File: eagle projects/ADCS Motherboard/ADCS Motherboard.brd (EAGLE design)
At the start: 91 x 91 mm, 144 parts, among them J1 HDR_10_EZFET_DEBUGGER, J11 CNC_3221-10-0300-00, J5 CNC_3221-10-0300-00, J7 TE-1734829-3, Q1 BSR802NL6327HTSA1, U1 MSP430F5529IPN, U10 TSV991AILT, U2 TSV991AILT, U3 ADS7841E_2K5, U4 TSV991AILT, U5 DMC4050SSDQ-13, U6 BNO055, U7 HMC1053, U9 BMX160, Y1 32.768kHz, Y2 CSTCR4M00G15L99, Y3 32.768kHz

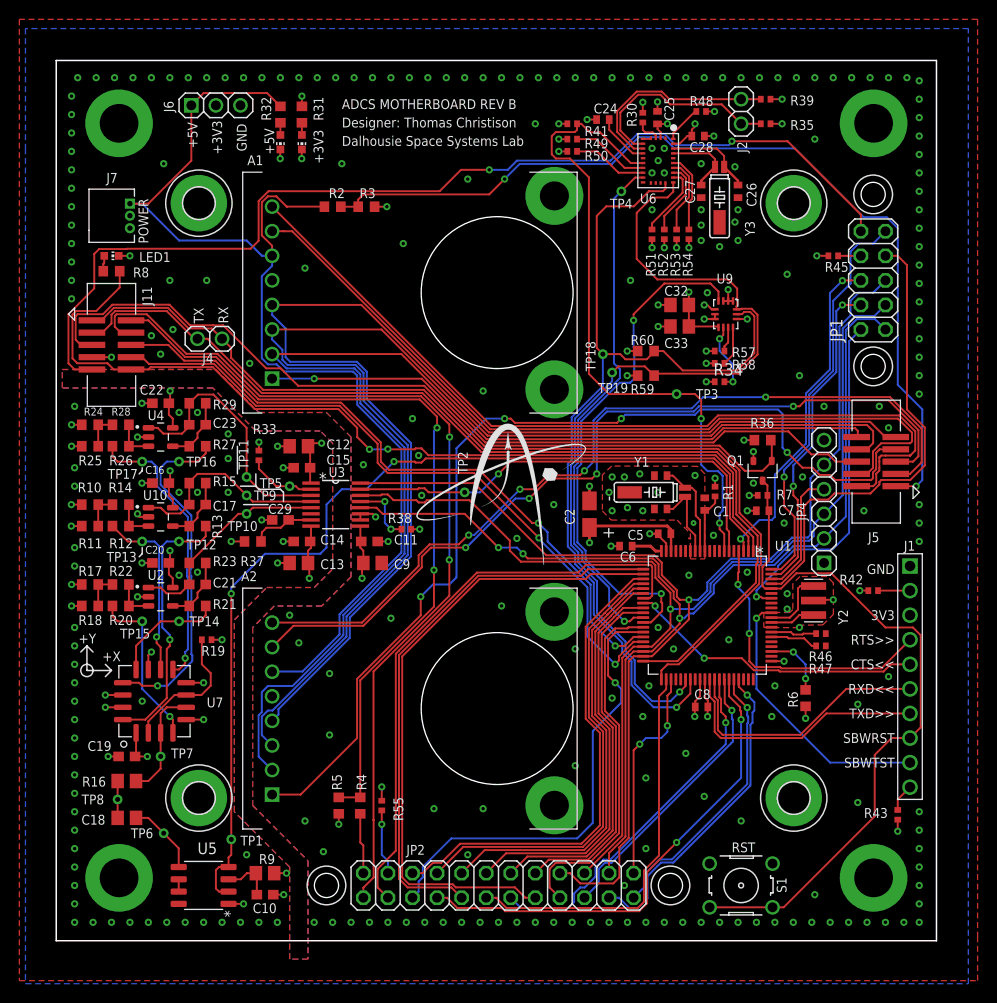
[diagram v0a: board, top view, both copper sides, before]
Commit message: silk screen
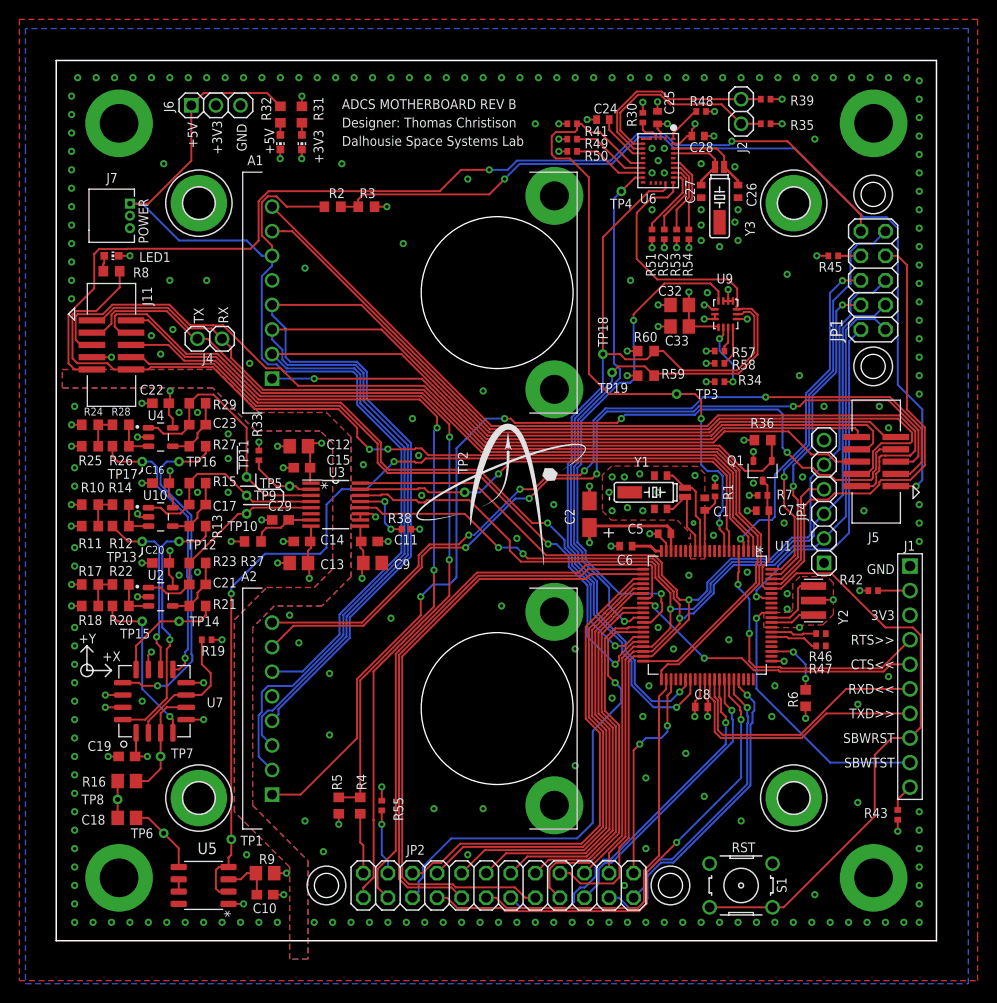
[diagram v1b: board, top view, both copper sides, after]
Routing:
- net UCB1_I2C_SCL: track 94.8 -> 92.6 mm
- net RESERVED_2: track 71.5 -> 72.2 mm
- net RESERVED_1: track 70.2 -> 70.7 mm

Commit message: finilized rev b layout
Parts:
- moved J6 16.6 mm to (14.6, 69.8), turned to 180 degrees
- moved R31 8.04 mm to (17.5, 84.1), turned to 0 degrees
- moved R32 6.70 mm to (17.5, 81.9), turned to 0 degrees
- moved LED2 5.32 mm to (20.3, 84.1), turned to 270 degrees
- moved LED3 2.93 mm to (20.3, 81.9), turned to 270 degrees
- moved LED1 0.95 mm to (4.76, 70.8)
- moved R8 0.95 mm to (4.76, 69.2)
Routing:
- net +5V: track 115.8 -> 105.6 mm
- net Z-_SUN_3V_PRESENT: track 107.5 -> 108.0 mm
- net GND: vias 311 -> 317
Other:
- outline, holes or cut-outs redrawn
- board text added: "*"

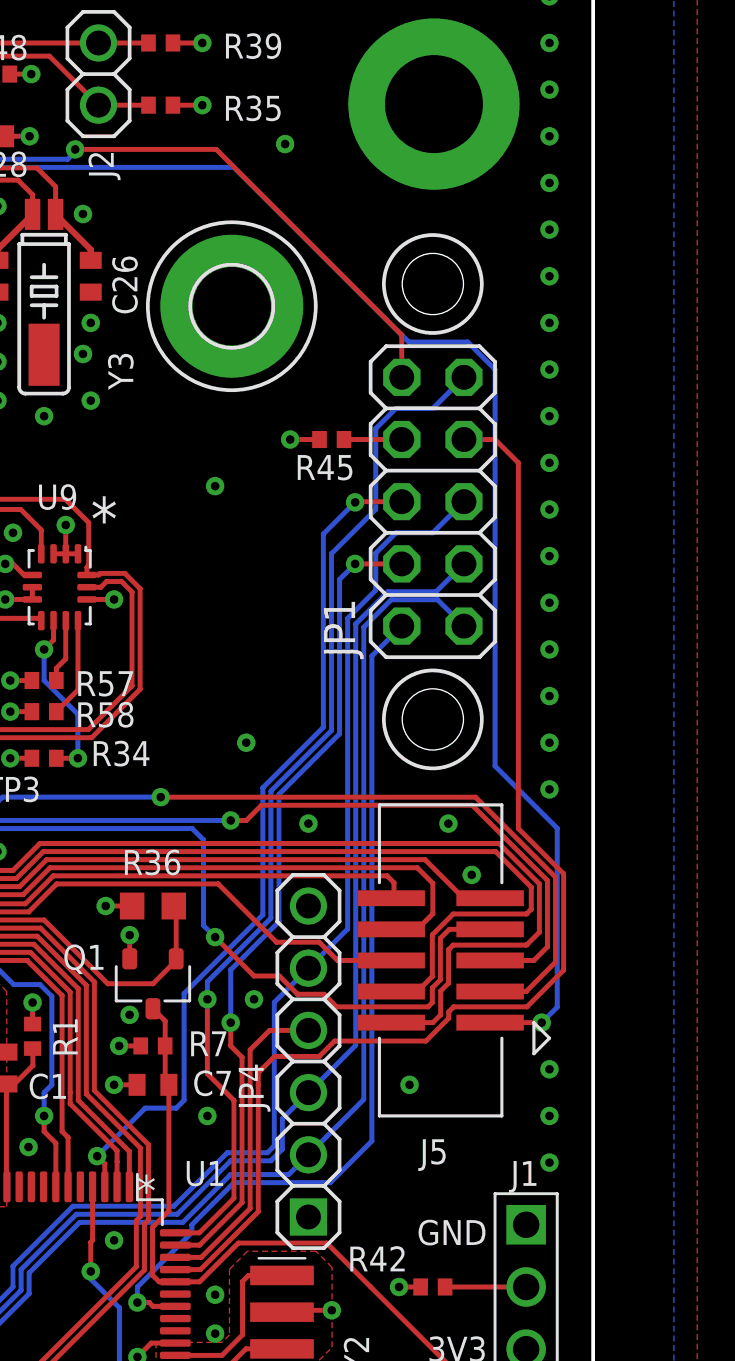
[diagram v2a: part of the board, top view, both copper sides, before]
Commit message: Solder Cups on Motherboard
Started swapping connectors on Motherboard
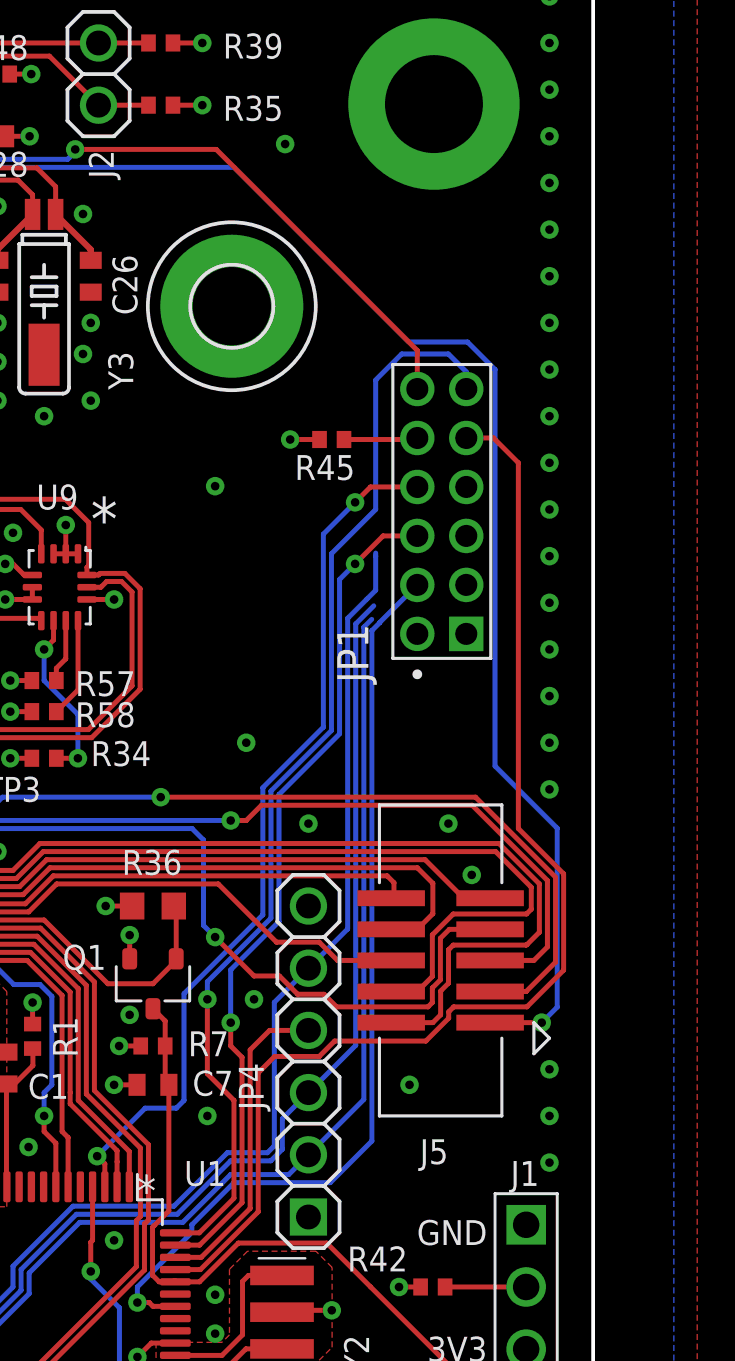
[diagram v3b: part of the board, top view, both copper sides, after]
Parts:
- JP1: value (none) -> 832-10-012-10-005000; device pinhead:2X05 -> 832-10-012-10-005000:832-10-012-10-005000
- moved JP1 5.43 mm to (83.8, 62.9)
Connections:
- net !CS!_SUN_X+: now also JP1.4; no longer JP1.2
- net !CS!_SUN_X-: now also JP1.9; no longer JP1.7
- net !CS!_SUN_Y+: now also JP1.6; no longer JP1.4
- net !CS!_SUN_Y-: now also JP1.11; no longer JP1.9
- net !CS!_SUN_Z-: now also JP1.8; no longer JP1.6
- net N$58: now also JP1.10; no longer JP1.8
- net UCB0_SPI_CLK: now also JP1.7; no longer JP1.5
- net UCB0_SPI_MISO: now also JP1.3; no longer JP1.1
- net UCB0_SPI_MOSI: now also JP1.5; no longer JP1.3
- net Z-_SUN_3V_PRESENT: now also JP1.12; no longer JP1.10
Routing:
- net UCB0_SPI_MISO: track 116.6 -> 112.0 mm
- net UCB0_SPI_CLK: track 126.0 -> 121.5 mm
- net UCB0_SPI_MOSI: track 118.2 -> 113.8 mm
- net !CS!_SUN_Y-: track 42.2 -> 44.8 mm
- net !CS!_SUN_X+: track 36.0 -> 38.0 mm
- net !CS!_SUN_Y+: track 33.7 -> 34.8 mm
- net !CS!_SUN_Z-: track 35.1 -> 36.0 mm
- net Z-_SUN_3V_PRESENT: track 108.0 -> 108.8 mm
- net N$58: track 2.36 -> 3.02 mm

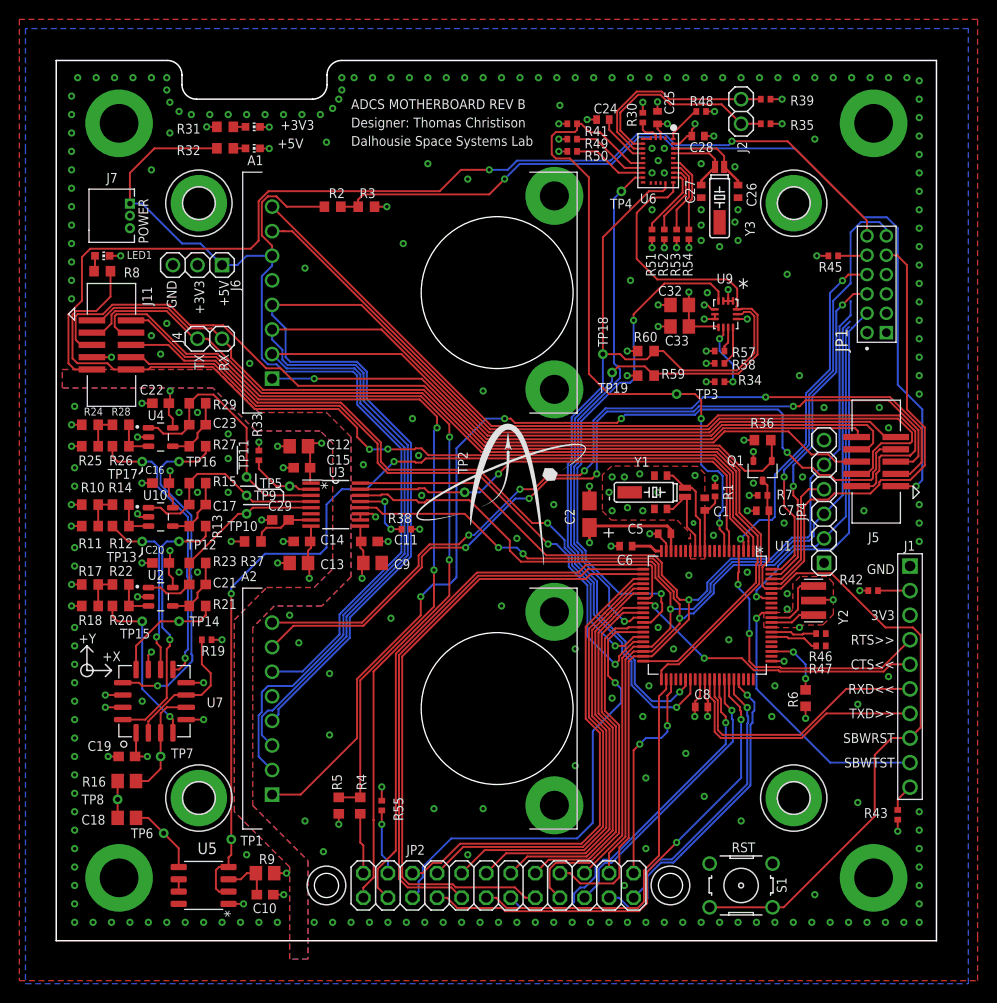
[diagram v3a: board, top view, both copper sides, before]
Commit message: Changed out OBC connector on motherboard
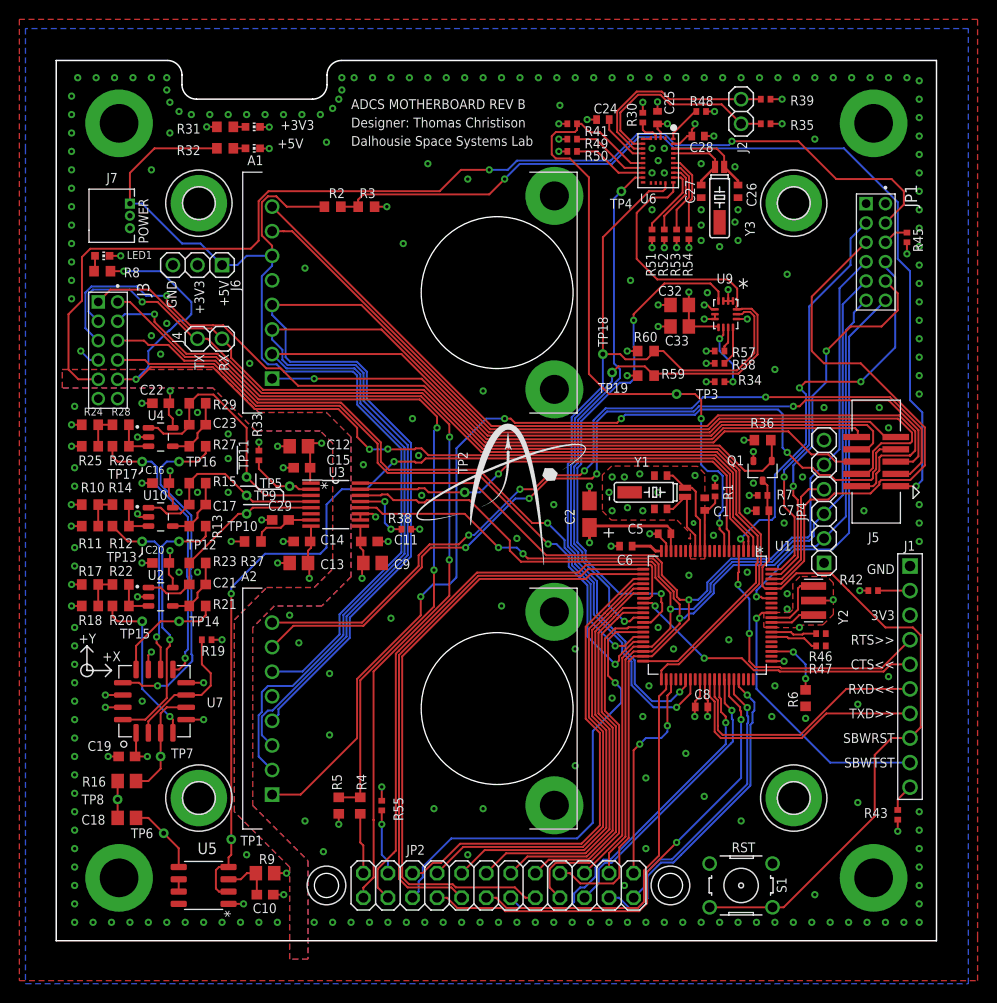
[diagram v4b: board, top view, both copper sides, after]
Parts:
- removed J11: CNC_3221-10-0300-00, my_library:CNC_3221-10-0300-00
- added J3: 832-10-012-10-005000, 832-10-012-10-005000:832-10-012-10-005000
- moved JP1 13.5 mm to (85.7, 76.2), turned to 270 degrees
- moved R45 7.85 mm to (87.9, 72.7), turned to 270 degrees
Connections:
- net !CS!_SUN_X+: now also JP1.12; no longer JP1.4
- net !CS!_SUN_X-: now also JP1.5; no longer JP1.9
- net !CS!_SUN_Y+: now also JP1.10; no longer JP1.6
- net !CS!_SUN_Y-: now also JP1.3; no longer JP1.11
- net +3V3: now also J3.7; no longer J11.7
- net ACT_BRD_3V_PRESENT: now also J3.4; no longer J11.4
- net ACT_BRD_5V_SHIFTED: now also J3.2; no longer J11.2
- net MSP430_ACTIVE: now also J3.10; no longer J11.10
- net MSP_OBC_RESET: now also J3.5; no longer J11.5
- net N$58: now also JP1.6; no longer JP1.10
- net RESERVED_1: now also J3.6; no longer J11.6
- net RESERVED_2: now also J3.8; no longer J11.8
- net UCA0RXD: now also J3.1; no longer J11.1
- net UCA0TXD: now also J3.3; no longer J11.3
- net UCB0_SPI_MISO: now also JP1.11; no longer JP1.3
- net UCB0_SPI_MOSI: now also JP1.9; no longer JP1.5
- net Z-_SUN_3V_PRESENT: now also J3.9, JP1.4; no longer J11.9, JP1.12
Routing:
- net !CS!_SUN_X-: track 48.4 -> 56.9 mm
- net Z-_SUN_3V_PRESENT: track 108.8 -> 115.3 mm
- net !CS!_SUN_Z-: track 36.0 -> 41.7 mm, vias 2 -> 3
- net UCB0_SPI_MOSI: track 113.8 -> 118.7 mm
- net UCB0_SPI_CLK: track 121.5 -> 126.2 mm
- net !CS!_SUN_Y+: track 34.8 -> 39.1 mm
- net MSP430_ACTIVE: track 94.9 -> 98.7 mm, vias 2 -> 4
- net !CS!_SUN_Y-: track 44.8 -> 41.3 mm
- net UCB0_SPI_MISO: track 112.0 -> 115.5 mm
- net UCA0TXD: track 102.4 -> 105.7 mm, vias 0 -> 1
- net ACT_BRD_3V_PRESENT: track 95.1 -> 92.4 mm, vias 2 -> 3
- net ACT_BRD_5V_SHIFTED: track 80.6 -> 82.8 mm
- net !CS!_SUN_X+: track 38.0 -> 40.1 mm
- net CAM_5V_PRESENT: track 95.0 -> 96.5 mm
- net RESERVED_1: track 70.7 -> 72.3 mm
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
